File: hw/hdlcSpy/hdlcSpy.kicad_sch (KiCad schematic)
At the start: 35 parts, among them J1 Conn_01x24_Pin, J2 Conn_01x09, U1 LM2936-5.0, U2 SN65HVD1782, U3 SN65HVD1782, U5 SN74LVC1G14DBV, U6 SN74LVC1G14DBV

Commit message: feat: cleanup schematic and pcb
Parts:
- R12: value 1K -> 10R
- R2, R3, R4, R5, R6, R7: value 1K -> 10K
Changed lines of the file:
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@@
 	)
 	(junction
-		(at 321.31 76.2)
+		(at 176.53 177.8)
 		(diameter 0)
 		(color 0 0 0 0)
 	)
 	(junction
-		(at 321.31 119.38)
+		(at 321.31 76.2)
 		(diameter 0)
 		(color 0 0 0 0)
 	)
 	(junction
-		(at 176.5208 177.8)
+		(at 321.31 119.38)
 		(diameter 0)
 		(color 0 0 0 0)
@@
 		(color 0 0 0 0)
 	)
-	(junction
-		(at 176.53 177.8)
-		(diameter 0)
-		(color 0 0 0 0)
-	)
 	(no_connect
 		(at 325.12 93.98)
@@
 	(wire
 		(pts
-			(xy 184.15 107.95) (xy 190.5 107.95)
+			(xy 176.53 179.07) (xy 176.53 177.8)
 		)
 		(stroke
@@
 	(wire
 		(pts
-			(xy 110.49 177.8) (xy 110.49 144.78)
+			(xy 184.15 107.95) (xy 190.5 107.95)
 		)
 		(stroke
@@
 	(wire
 		(pts
-			(xy 269.24 69.85) (xy 270.51 69.85)
+			(xy 110.49 177.8) (xy 110.49 144.78)
 		)
 		(stroke
@@
 	(wire
 		(pts
-			(xy 300.99 81.28) (xy 300.99 114.3)
+			(xy 269.24 69.85) (xy 270.51 69.85)
 		)
 		(stroke
@@
 	(wire
 		(pts
-			(xy 176.53 177.8) (xy 176.53 179.07)
+			(xy 300.99 81.28) (xy 300.99 114.3)
 		)
 		(stroke
@@
 	(wire
 		(pts
+			(xy 176.53 177.8) (xy 172.72 177.8)
+		)
+		(stroke
+			(width 0)
+			(type default)
+		)
+	)
+	(wire
+		(pts
 			(xy 152.4 186.69) (xy 152.4 190.5)
 		)
@@
 	(wire
 		(pts
-			(xy 172.72 177.8) (xy 176.5208 177.8)
-		)
-		(stroke
-			(width 0)
-			(type default)
-		)
-	)
-	(wire
-		(pts
 			(xy 218.44 118.11) (xy 248.92 118.11)
 		)
@@
 	(wire
 		(pts
-			(xy 176.53 177.8) (xy 181.61 177.8)
-		)
-		(stroke
-			(width 0)
-			(type default)
-		)
-	)
-	(wire
-		(pts
 			(xy 273.05 106.68) (xy 273.05 107.95)
 		)
@@
 	(wire
 		(pts
-			(xy 176.5208 177.8) (xy 176.53 177.8)
+			(xy 240.03 67.31) (xy 248.92 67.31)
 		)
 		(stroke
@@
 	(wire
 		(pts
-			(xy 240.03 67.31) (xy 248.92 67.31)
+			(xy 270.51 74.93) (xy 270.51 77.47)
 		)
 		(stroke
@@
 	(wire
 		(pts
-			(xy 270.51 74.93) (xy 270.51 77.47)
+			(xy 218.44 67.31) (xy 240.03 67.31)
 		)
 		(stroke
@@
 	(wire
 		(pts
-			(xy 218.44 67.31) (xy 240.03 67.31)
+			(xy 321.31 121.92) (xy 321.31 119.38)
 		)
 		(stroke
@@
 	(wire
 		(pts
-			(xy 321.31 121.92) (xy 321.31 119.38)
+			(xy 176.53 177.8) (xy 181.61 177.8)
 		)
 		(stroke
@@
 			)
 		)
-		(property "Value" "1K"
+		(property "Value" "10K"
 			(at 273.05 61.976 90)
 			(show_name no)
@@
 	(symbol
 		(lib_id "power:PWR_FLAG")
-		(at 176.5208 177.8 0)
+		(at 176.53 177.8 0)
 		(unit 1)
 		(body_style 1)
@@
 		(fields_autoplaced yes)
 		(property "Reference" "#FLG06"
-			(at 176.2668 177.8 0)
+			(at 176.276 177.8 0)
 			(hide yes)
 			(show_name no)
@@
 		)
 		(property "Value" "PWR_FLAG"
-			(at 176.7748 175.514 0)
+			(at 176.784 175.514 0)
 			(hide yes)
 			(show_name no)
@@
 		)
 		(property "Footprint" ""
-			(at 176.5208 177.8 0)
+			(at 176.53 177.8 0)
 			(hide yes)
 			(show_name no)
@@
 		)
 		(property "Datasheet" ""
-			(at 176.5208 176.276 0)
+			(at 176.53 176.276 0)
 			(hide yes)
 			(show_name no)
@@
 		)
 		(property "Description" "Special symbol for telling ERC where power comes from"
-			(at 177.2828 157.48 0)
+			(at 177.292 157.48 0)
 			(hide yes)
 			(show_name no)
@@
 			)
 		)
-		(property "Value" "1K"
+		(property "Value" "10K"
 			(at 273.05 122.936 90)
 			(show_name no)
@@
 		(property "Value" "VLMTG1400-GS08"
 			(at 111.252 190.5 90)
+			(hide yes)
 			(show_name no)
 			(do_not_autoplace no)
@@
 		(dnp no)
 		(property "Reference" "R12"
-			(at 185.42 176.276 0)
+			(at 185.42 175.768 90)
 			(show_name no)
 			(do_not_autoplace no)
@@
 					(size 1.27 1.27)
 				)
-				(justify left)
 			)
 		)
-		(property "Value" "1K"
+		(property "Value" "10R"
 			(at 185.166 177.8 90)
 			(show_name no)
@@
 		(property "Value" "VLMTG1400-GS08"
 			(at 117.094 190.5 90)
+			(hide yes)
 			(show_name no)
 			(do_not_autoplace no)
@@
 			)
 		)
-		(property "Value" "1K"
+		(property "Value" "10K"
 			(at 273.05 112.776 90)
 			(show_name no)
@@
 			)
 		)
-		(property "Value" "1K"
+		(property "Value" "10K"
 			(at 273.05 72.136 90)
 			(show_name no)
@@
 		(property "Value" "VLMTG1400-GS08"
 			(at 131.318 190.5 90)
+			(hide yes)
 			(show_name no)
 			(do_not_autoplace no)
@@
 		(property "Value" "VLMTG1400-GS08"
 			(at 123.698 190.5 90)
+			(hide yes)
 			(show_name no)
 			(do_not_autoplace no)
@@
 			)
 		)
-		(property "Value" "1K"
+		(property "Value" "10K"
 			(at 273.05 82.296 90)
 			(show_name no)
@@
 			)
 		)
-		(property "Value" "1K"
+		(property "Value" "10K"
 			(at 273.05 102.616 90)
 			(show_name no)

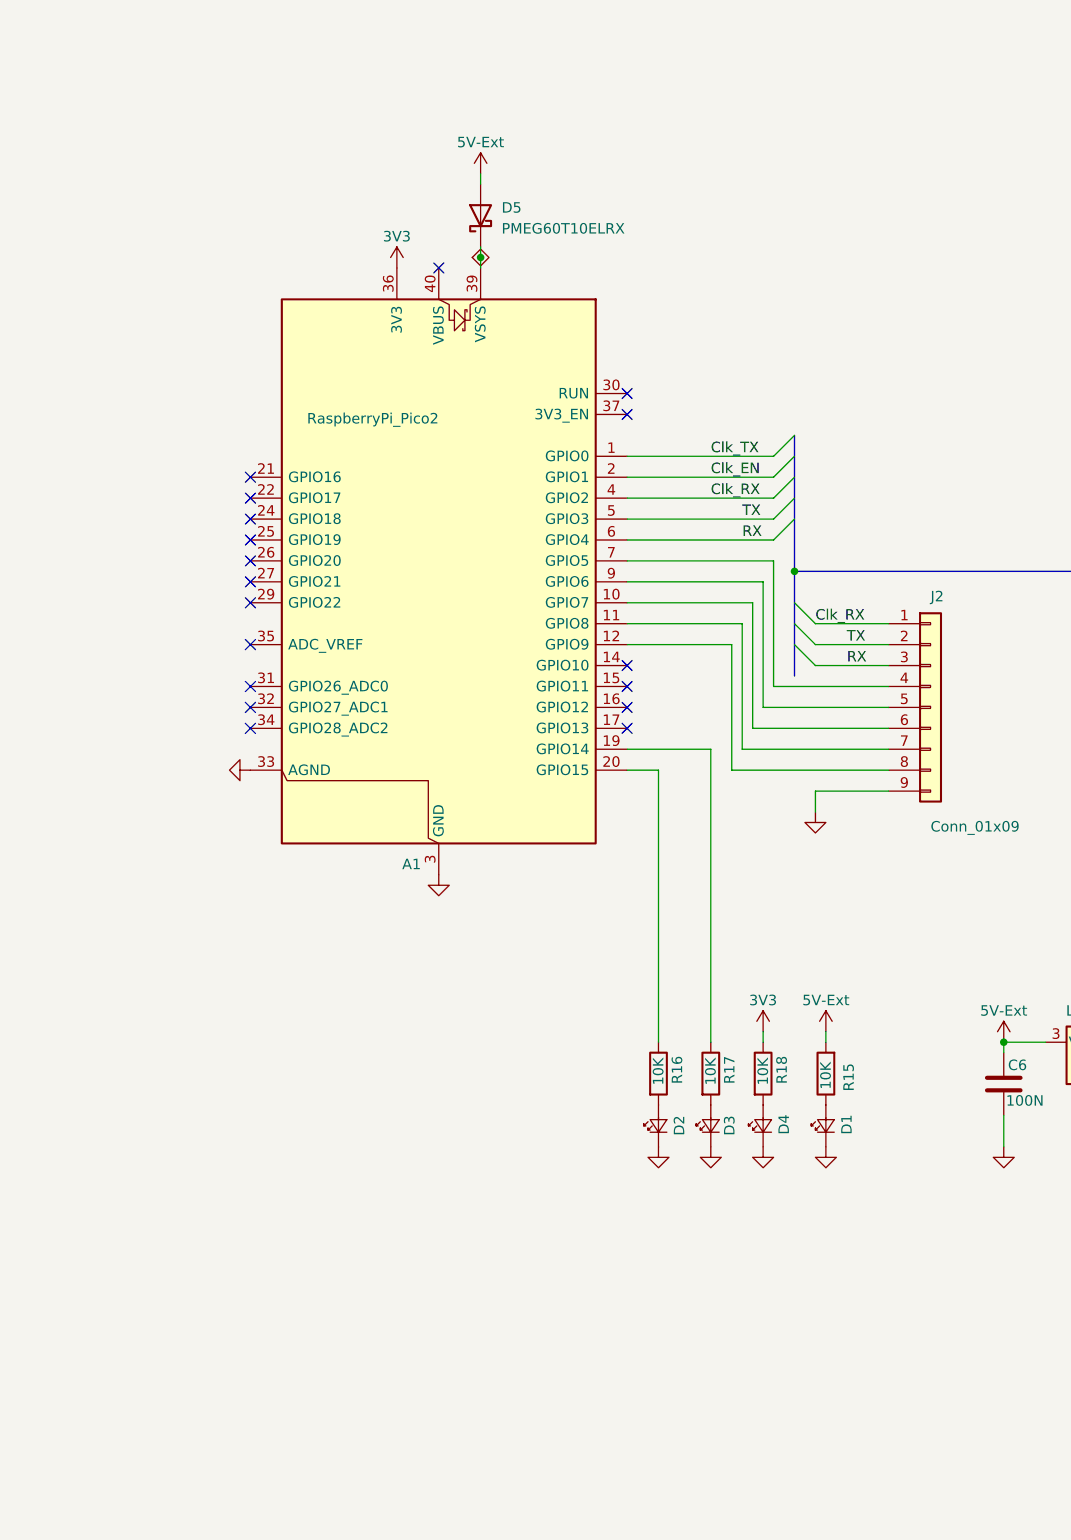
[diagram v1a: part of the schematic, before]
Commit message: feat: add sdcard to hw
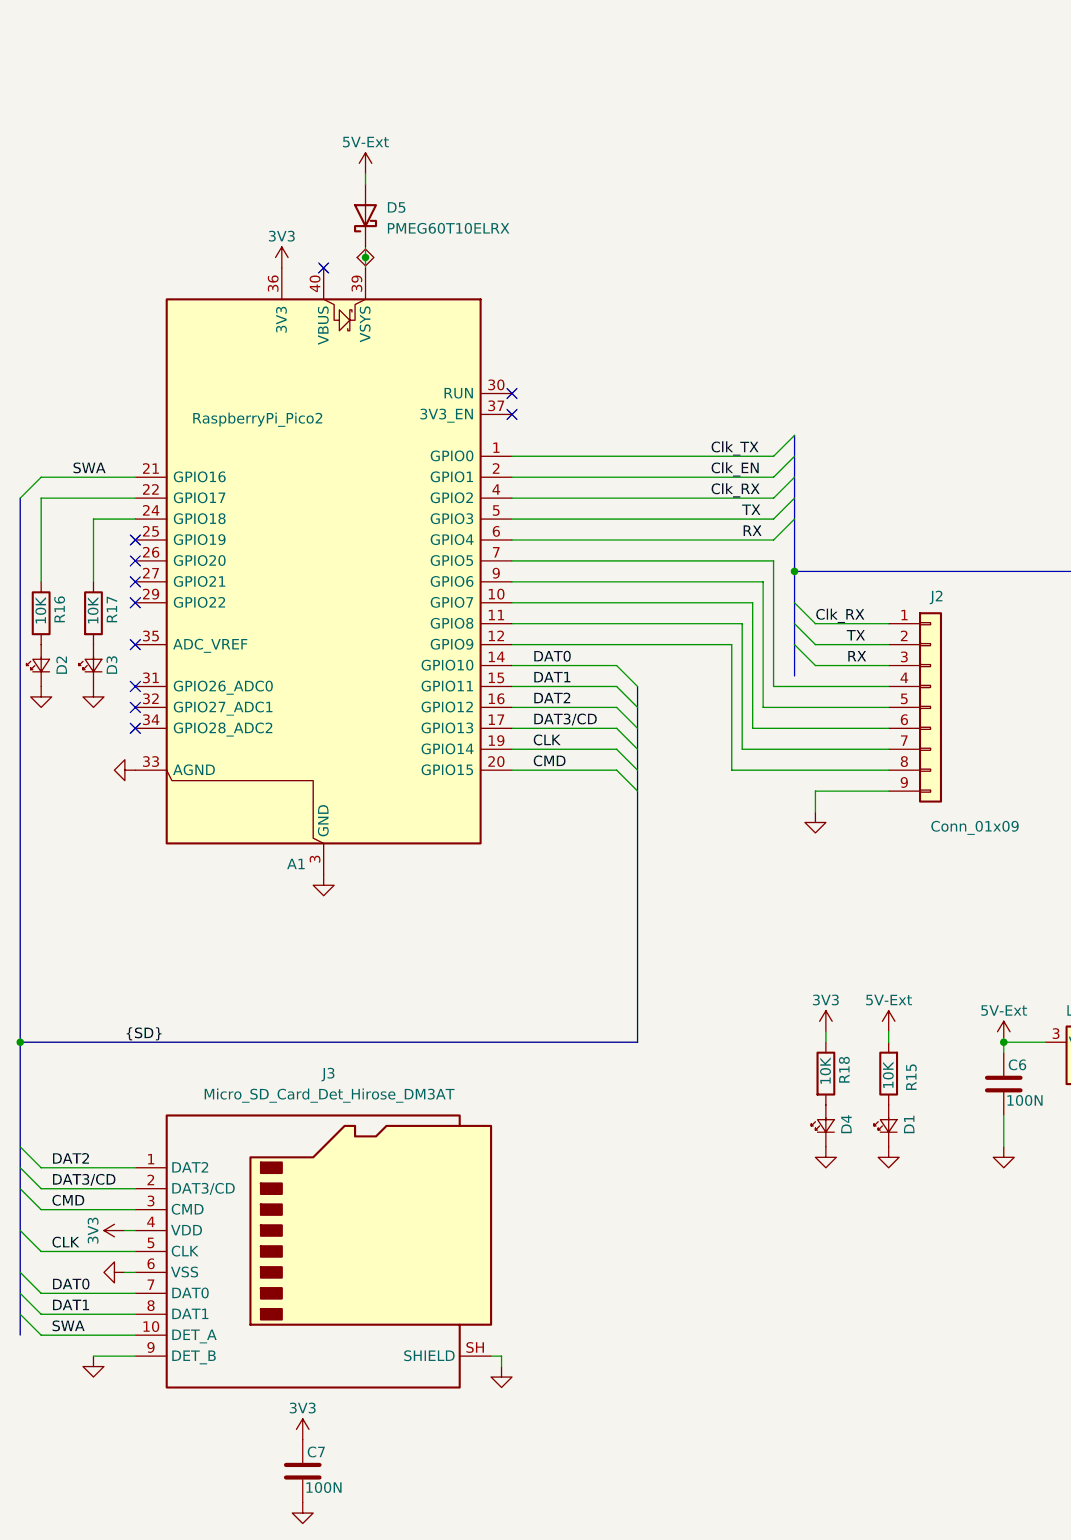
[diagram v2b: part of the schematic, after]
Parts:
- added C7: 100N, Capacitor_SMD:C_0603_1608Metric_Pad1.08x0.95mm_HandSolder, symbol Device:C
- added J3: Micro_SD_Card_Det_Hirose_DM3AT, Connector_Card:microSD_HC_Hirose_DM3D-SF, symbol Connector:Micro_SD_Card_Det_Hirose_DM3AT
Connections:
- net 3V3: now also C7.1, J3.4 (VDD)
- net GND: now also C7.2, J3.6 (VSS), J3.9 (DET_B), J3.SH (SHIELD)
- net at R17.1: now also A1.24 (GPIO18); no longer A1.19 (GPIO14)
- net at R16.1: now also A1.22 (GPIO17); no longer A1.20 (GPIO15)
- net DAT0: now reaches A1.14 (GPIO10)
- net DAT0: now also J3.7 (DAT0)
- net DAT1: now reaches A1.15 (GPIO11)
- net DAT1: now also J3.8 (DAT1)
- net DAT2: now reaches A1.16 (GPIO12)
- net DAT2: now also J3.1 (DAT2)
- net DAT3/CD: now reaches A1.17 (GPIO13)
- net DAT3/CD: now also J3.2 (DAT3/CD)
- net SWA: now reaches A1.21 (GPIO16)
- net SWA: now also J3.10 (DET_A)
- new net CLK: A1.19 (GPIO14), J3.5 (CLK)
- new net CMD: A1.20 (GPIO15), J3.3 (CMD)
- no-connect marks 30 -> 23
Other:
- moved on the sheet: A1, D1, D2, D3, D4, D5, R15, R16, R17, R18

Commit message: feat: sch and pcb done
Add some Datasheets
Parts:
- J1: value Conn_01x24_Pin -> MODULBUS
- J3: footprint Connector_Card:microSD_HC_Hirose_DM3D-SF -> DM3CS-SF; DigiKey (none) -> HR1972CT-ND
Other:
- company: (none) -> Embedded-Bonjour GmbH
- title: hdlcSpy -> ${PROJECTNAME}
- moved on the sheet: A1, C1, C2, C3, C4, C5, C6, C7, D1, D2, D3, D4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

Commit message: feat: orderd at Jjlcpcb
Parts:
- J1: value MODULBUS -> PIN HEADER 2.0MM PITCH STR SMT,2; footprint Connector_PinHeader_2.00mm:PinHeader_2x12_P2.00mm_Vertical_SMD -> G825M24401YEU; DigiKey (none) -> 664-G825M24401YEUTR-ND
- J2: value Conn_01x09 -> Connector_PinHeader_2.54mm:PinHeader_1x09_P2.54mm_Vertical
- U2, U3: value SN65HVD1782 -> ST4E1240DT
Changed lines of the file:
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@@
 			)
 		)
-		(property "Value" "SN65HVD1782"
+		(property "Value" "ST4E1240DT"
 			(at 281.686 81.788 0)
 			(show_name no)
@@
 			)
 		)
-		(property "Value" "Conn_01x09"
+		(property "Value" "Connector_PinHeader_2.54mm:PinHeader_1x09_P2.54mm_Vertical"
 			(at 173.99 136.398 0)
 			(show_name no)
@@
 			)
 		)
-		(property "Value" "SN65HVD1782"
+		(property "Value" "ST4E1240DT"
 			(at 273.304 45.72 0)
 			(show_name no)
@@
 			)
 		)
-		(property "Value" "MODULBUS"
+		(property "Value" "PIN HEADER 2.0MM PITCH STR SMT,2"
 			(at 362.712 83.82 0)
 			(show_name no)
@@
 			)
 		)
-		(property "Footprint" "Connector_PinHeader_2.00mm:PinHeader_2x12_P2.00mm_Vertical_SMD"
+		(property "Footprint" "G825M24401YEU"
 			(at 360.68 81.28 0)
 			(hide yes)
@@
 			)
 		)
-		(property "DigiKey" ""
+		(property "DigiKey" "664-G825M24401YEUTR-ND"
 			(at 360.68 81.28 0)
 			(hide yes)
